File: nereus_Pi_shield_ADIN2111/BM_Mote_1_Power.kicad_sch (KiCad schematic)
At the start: 14 parts, among them U5 LMR51430YDDCR, U6 TPS62840YBGR

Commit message: S4.a: 5 V converter for the Pi (U10, copy of U5); close S3
Power sheet: U5 block copied with schedit.copy_block (new refs U10, L6,
C53-C58, R37-R40); R38 13.7k (5 V), C56/C57 22uF 16V 0805 + C58 4.7uF
10V 0402; L6 same PA5432.822NLT. Top-Level: 5V_PI sheet pin, TP38, label;
TP23/TP24 moved down to clear it. DESIGN D13. ERC 78/629, netcheck 53/53,
existing parts' connections identical.

Co-Authored-By: Claude Opus 5.5 <noreply@anthropic.com>
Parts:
- added C53: CL05A104KA5NNNC, FP-CL278-IPC_C, symbol BM_Mote_000639-AB-altium-import:POWER_3_b4654b650e69147ec39a6b967a45e02_Altium 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
- added C54: GRM188R72A104KA35D, FP-GRM188-0_1-e0_2_0_5-IPC_B, symbol BM_Mote_000639-AB-altium-import:POWER_0_11868f565c42a9108669ba33697ecf6_Altium 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
- added C55: UMK107BBJ225KA-T, FP-0603-L_1_6_0_2-W_0_8_0-MFG, symbol BM_Mote_000639-AB-altium-import:POWER_0_b4654b650e69147ec39a6b967a45e02_Altium 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
- added C56, C57: GRM21BR61C226ME44L, Capacitor_SMD:C_0805_2012Metric, symbol BM_Mote_000639-AB-altium-import:POWER_1_CAP-NP-2_Altium Content Vault
- added C58: GRM155R61A475MEAAD, Capacitor_SMD:C_0402_1005Metric, symbol BM_Mote_000639-AB-altium-import:POWER_0_b4654b650e69147ec39a6b967a45e02_Altium 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
- added L6: PA5432.822NLT, FP-PA5432_472NLT-MFG, symbol BM_Mote_000639-AB-altium-import:POWER_0_725321dda6339637d4d059423bc1c3c_Sofar O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
- added R37: RMCF0402FT100K, FP-RMCF0402-IPC_C, symbol BM_Mote_000639-AB-altium-import:POWER_3_1029c3af85768c4190bb7ad29bc67b5_Altium 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
- added R38: RC0402FR-0713K7L, FP-RC0402-0_4-IPC_B, symbol BM_Mote_000639-AB-altium-import:POWER_3_1029c3af85768c4190bb7ad29bc67b5_Altium 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
- added R39: CRCW04021M82FKED, FP-CRCW0402-e3-MFG, symbol BM_Mote_000639-AB-altium-import:POWER_1_1029c3af85768c4190bb7ad29bc67b5_Altium 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
- added R40: RC0402FR-07200KL, RESC1005X40X25LL05T10, symbol BM_Mote_000639-AB-altium-import:POWER_1_RES_Altium Content Vault_0
- added U10: LMR51430YDDCR, SOT-23-THIN-6_DDC_TEX, symbol BM_Mote_000639-AB-altium-import:POWER_0_LMR51430YDDCR_Sofar Ocean Technologies,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

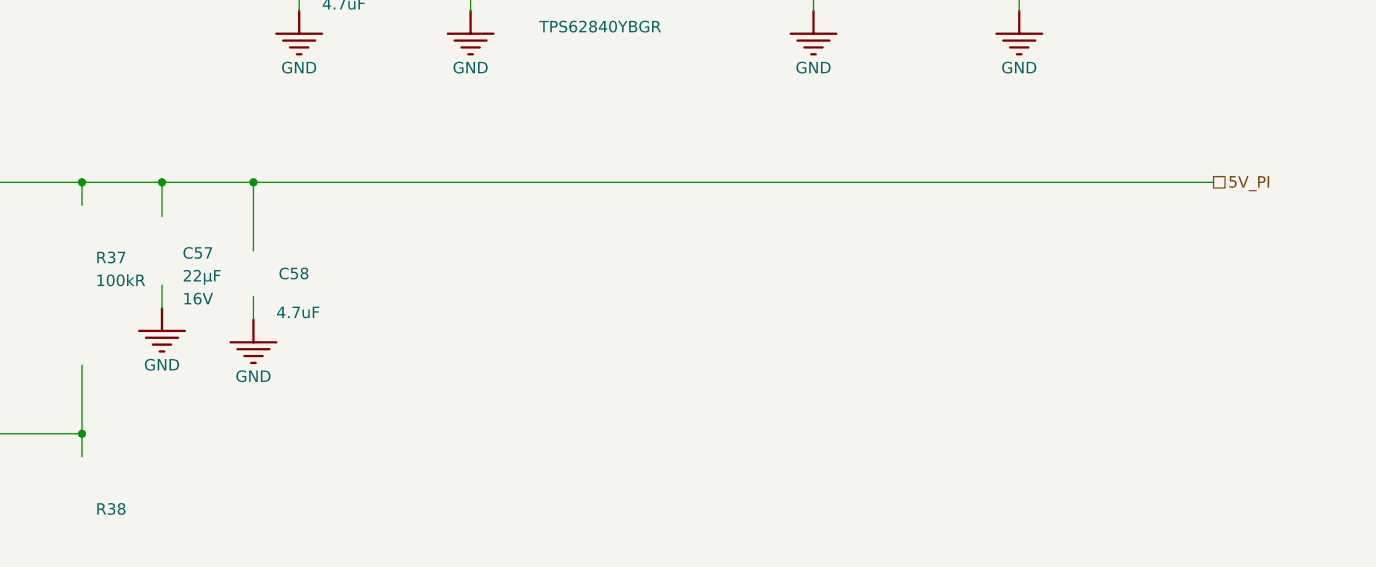
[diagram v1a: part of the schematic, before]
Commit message: S4.a: fix QE round 1 (set_properties escaped quotes, C56/C57 stale fields, docs)
F1: PROP regex accepts escaped chars; set_properties refuses partial
parses; test added; stale 0603 fields removed from C56/C57. F2 thermal
item in S4.c + SPEC; F3 demo line; F4-F7 D13/SPEC; F8 C58 one grid right
with 10V shown. Connectivity and values unchanged. Report in qe/S4.md.

Co-Authored-By: Claude Opus 5.5 <noreply@anthropic.com>
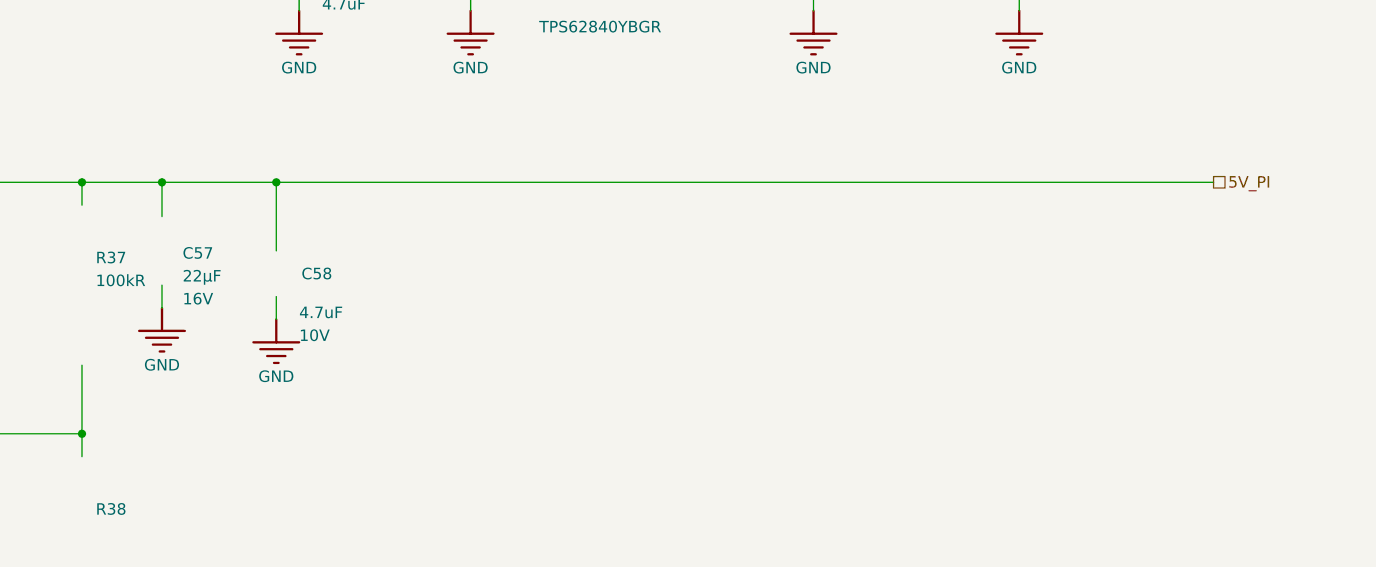
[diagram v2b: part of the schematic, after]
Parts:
- C56, C57: SIZE / DIMENSION 0.063"Lx0.031"W(1.60mmx0.80mm) -> (none); THICKNESS (MAX) 0.039"(1.00mm) -> (none)
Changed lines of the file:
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@@
 	)
 	(junction
-		(at 251.46 210.6422)
+		(at 254 210.6422)
 		(diameter 0)
 		(color 0 0 0 0)
@@
 	(wire
 		(pts
-			(xy 251.46 225.8822) (xy 251.46 223.3422)
+			(xy 254 225.8822) (xy 254 223.3422)
 		)
 		(stroke
@@
 	(wire
 		(pts
-			(xy 241.3 210.6422) (xy 251.46 210.6422)
+			(xy 241.3 210.6422) (xy 254 210.6422)
 		)
 		(stroke
@@
 	(wire
 		(pts
-			(xy 251.46 210.6422) (xy 358.14 210.6422)
+			(xy 254 210.6422) (xy 358.14 210.6422)
 		)
 		(stroke
@@
 	(wire
 		(pts
-			(xy 251.46 210.6422) (xy 251.46 218.2622)
+			(xy 254 210.6422) (xy 254 218.2622)
 		)
 		(stroke
@@
 			)
 		)
-		(property "THICKNESS (MAX)" "0.039\"(1.00mm)"
-			(at 203.454 213.9442 0)
-			(effects
-				(font
-					(size 1.27 1.27)
-				)
-				(justify left bottom)
-				(hide yes)
-			)
-		)
 		(property "CAPACITANCE" "22µF"
 			(at 208.026 221.8182 0)
@@
 			)
 		)
-		(property "SIZE / DIMENSION" "0.063\"Lx0.031\"W(1.60mmx0.80mm)"
-			(at 203.454 213.9442 0)
-			(effects
-				(font
-					(size 1.27 1.27)
-				)
-				(justify left bottom)
-				(hide yes)
-			)
-		)
 		(pin "1"
 		)
@@
 			)
 		)
-		(property "THICKNESS (MAX)" "0.039\"(1.00mm)"
-			(at 239.014 213.9442 0)
-			(effects
-				(font
-					(size 1.27 1.27)
-				)
-				(justify left bottom)
-				(hide yes)
-			)
-		)
 		(property "CAPACITANCE" "22µF"
 			(at 243.586 221.8182 0)
@@
 			)
 		)
-		(property "SIZE / DIMENSION" "0.063\"Lx0.031\"W(1.60mmx0.80mm)"
-			(at 239.014 213.9442 0)
-			(effects
-				(font
-					(size 1.27 1.27)
-				)
-				(justify left bottom)
-				(hide yes)
-			)
-		)
 		(pin "1"
 		)
@@
 	(symbol
 		(lib_id "BM_Mote_000639-AB-altium-import:POWER_0_b4654b650e69147ec39a6b967a45e02_Altium Content Vault")
-		(at 251.46 218.2622 0)
+		(at 254 218.2622 0)
 		(unit 0)
 		(exclude_from_sim no)
@@
 		(dnp no)
 		(property "Reference" "C58"
-			(at 254.254 221.5642 0)
+			(at 256.794 221.5642 0)
 			(effects
 				(font
@@
 		)
 		(property "Value" "GRM155R61A475MEAAD"
-			(at 254.254 224.1042 0)
+			(at 256.794 224.1042 0)
 			(effects
 				(font
@@
 		)
 		(property "Footprint" "Capacitor_SMD:C_0402_1005Metric"
-			(at 251.46 218.2622 0)
+			(at 254 218.2622 0)
 			(effects
 				(font
@@
 		)
 		(property "Datasheet" ""
-			(at 251.46 218.2622 0)
+			(at 254 218.2622 0)
 			(effects
 				(font
@@
 		)
 		(property "Description" "Chip Capacitor, 4.7 uF, +/- 20%, 10 V, X5R, -55 to 85 degC, 0402 (1005 Metric)"
-			(at 251.46 218.2622 0)
+			(at 254 218.2622 0)
 			(effects
 				(font
@@
 		)
 		(property "CASE/PACKAGE" "0402"
-			(at 248.666 217.7542 0)
+			(at 251.206 217.7542 0)
 			(effects
 				(font
@@
 		)
 		(property "CAPACITANCE" "4.7uF"
-			(at 254 225.8822 0)
+			(at 256.54 225.8822 0)
 			(effects
 				(font
@@
 		)
 		(property "TOLERANCE" "20%"
-			(at 248.666 217.7542 0)
+			(at 251.206 217.7542 0)
 			(effects
 				(font
@@
 		)
 		(property "DIELECTRIC" "X5R"
-			(at 248.666 217.7542 0)
+			(at 251.206 217.7542 0)
 			(effects
 				(font
@@
 		)
 		(property "VOLTAGE RATING" "10V"
-			(at 248.666 217.7542 0)
+			(at 256.54 228.4222 0)
 			(effects
 				(font
@@
 				)
 				(justify left bottom)
-				(hide yes)
 			)
 		)
 		(property "MANUFACTURER" "Murata"
-			(at 251.46 218.2622 0)
+			(at 254 218.2622 0)
 			(effects
 				(font
@@
 		)
 		(property "DATASHEET URL" "https://pim.murata.com/en-us/pim/details/?partNum=GRM155R61A475MEAA%23"
-			(at 251.46 218.2622 0)
+			(at 254 218.2622 0)
 			(effects
 				(font
@@
 	(symbol
 		(lib_id "BM_Mote_000639-AB-altium-import:GND_POWER_GROUND")
-		(at 251.46 225.8822 0)
+		(at 254 225.8822 0)
 		(unit 1)
 		(exclude_from_sim no)
@@
 		(dnp no)
 		(property "Reference" "#PWR75"
-			(at 251.46 225.8822 0)
+			(at 254 225.8822 0)
 			(effects
 				(font
@@
 		)
 		(property "Value" "GND"
-			(at 251.46 232.2322 0)
+			(at 254 232.2322 0)
 			(effects
 				(font
@@
 		)
 		(property "Footprint" ""
-			(at 251.46 225.8822 0)
+			(at 254 225.8822 0)
 			(effects
 				(font
@@
 		)
 		(property "Datasheet" ""
-			(at 251.46 225.8822 0)
+			(at 254 225.8822 0)
 			(effects
 				(font
@@
 		)
 		(property "Description" ""
-			(at 251.46 225.8822 0)
+			(at 254 225.8822 0)
 			(effects
 				(font
